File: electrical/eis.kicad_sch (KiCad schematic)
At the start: 7 parts

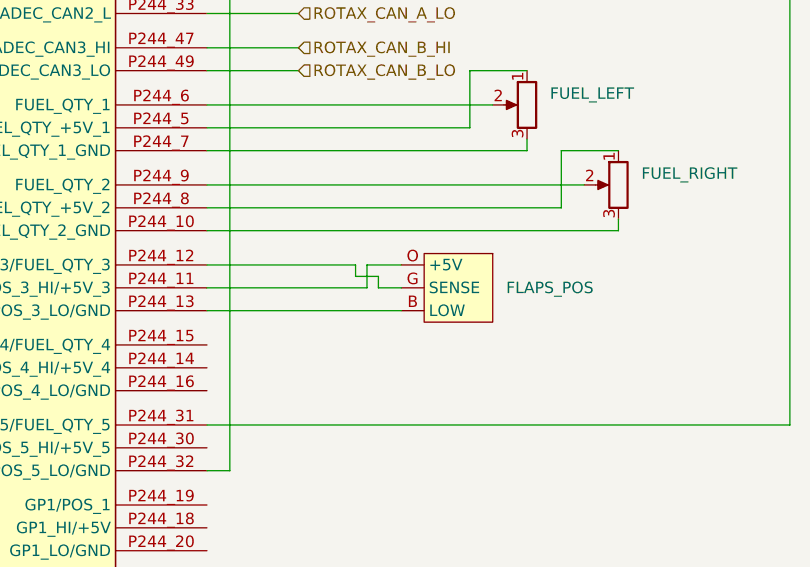
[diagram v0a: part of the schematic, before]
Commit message: Switch Slats to use Roll and put Flaps on Flaps.
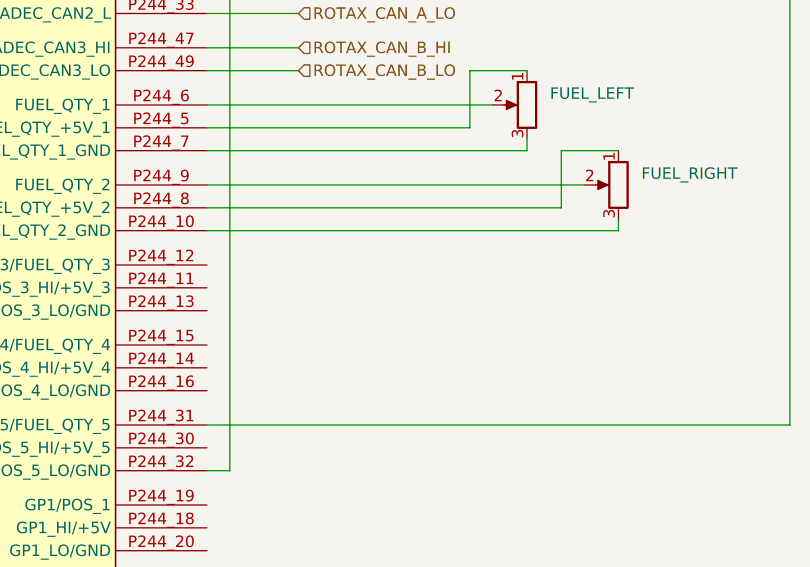
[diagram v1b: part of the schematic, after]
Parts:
- removed FLAPS_POS: ~, symbol flyerx:Ray_Allen_POS-12
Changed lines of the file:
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@@
   (title_block
     (title "EIS")
-    (date "2024-02-13")
-    (rev "0.9.1")
+    (date "2024-03-15")
+    (rev "0.9.2")
     (company "N915SN Angry Bird")
   )
@@
     (stroke (width 0) (type default))
   )
-  (wire (pts (xy 67.31 251.46) (xy 85.09 251.46))
-    (stroke (width 0) (type default))
-  )
   (wire (pts (xy 95.25 33.02) (xy 102.87 33.02))
     (stroke (width 0) (type default))
@@
     (stroke (width 0) (type default))
   )
-  (wire (pts (xy 67.31 254) (xy 88.9 254))
-    (stroke (width 0) (type default))
-  )
   (wire (pts (xy 67.31 190.5) (xy 69.85 190.5))
     (stroke (width 0) (type default))
@@
     (stroke (width 0) (type default))
   )
-  (wire (pts (xy 86.36 251.46) (xy 86.36 250.19))
-    (stroke (width 0) (type default))
-  )
   (wire (pts (xy 67.31 187.96) (xy 137.16 187.96))
     (stroke (width 0) (type default))
@@
     (stroke (width 0) (type default))
   )
-  (wire (pts (xy 86.36 251.46) (xy 88.9 251.46))
-    (stroke (width 0) (type default))
-  )
   (wire (pts (xy 90.17 121.92) (xy 92.71 121.92))
     (stroke (width 0) (type default))
@@
     (stroke (width 0) (type default))
   )
-  (wire (pts (xy 67.31 248.92) (xy 83.82 248.92))
-    (stroke (width 0) (type default))
-  )
   (wire (pts (xy 113.03 245.11) (xy 113.03 243.84))
     (stroke (width 0) (type default))
@@
     (stroke (width 0) (type default))
   )
-  (wire (pts (xy 85.09 248.92) (xy 88.9 248.92))
-    (stroke (width 0) (type default))
-  )
   (wire (pts (xy 67.31 240.03) (xy 109.22 240.03))
     (stroke (width 0) (type default))
@@
     (stroke (width 0) (type default))
   )
-  (wire (pts (xy 83.82 248.92) (xy 83.82 250.19))
-    (stroke (width 0) (type default))
-  )
   (wire (pts (xy 67.31 245.11) (xy 113.03 245.11))
     (stroke (width 0) (type default))
   )
-  (wire (pts (xy 83.82 250.19) (xy 86.36 250.19))
-    (stroke (width 0) (type default))
-  )
   (wire (pts (xy 67.31 220.98) (xy 77.47 220.98))
     (stroke (width 0) (type default))
@@
   )
   (wire (pts (xy 106.68 236.22) (xy 113.03 236.22))
-    (stroke (width 0) (type default))
-  )
-  (wire (pts (xy 85.09 251.46) (xy 85.09 248.92))
     (stroke (width 0) (type default))
   )
@@
     (effects (font (size 1.27 1.27)) (justify left))
   )
-  (symbol (lib_id "flyerx:Ray_Allen_POS-12") (at 99.06 247.65 0) (mirror y) (unit 1)
-    (in_bom yes) (on_board yes) (dnp no)
-    (property "Reference" "FLAPS_POS" (at 105.41 251.46 0)
-      (effects (font (size 1.27 1.27)))
-    )
-    (property "Value" "~" (at 105.41 245.11 0)
-      (effects (font (size 1.27 1.27)))
-    )
-    (property "Footprint" "" (at 105.41 245.11 0)
-      (effects (font (size 1.27 1.27)) hide)
-    )
-    (property "Datasheet" "" (at 105.41 245.11 0)
-      (effects (font (size 1.27 1.27)) hide)
-    )
-    (pin "B")
-    (pin "G")
-    (pin "O")
-    (instances
-      (project "electrical"
-        (path "/e8ec215a-dbe2-4eba-a577-e50a0a128049/72184f52-5cc1-469a-bd6f-4bd63aea59bf"
-          (reference "FLAPS_POS") (unit 1)
-        )
-      )
-    )
-  )
   (symbol (lib_id "flyerx:Kavlico_P4055") (at 100.33 115.57 0) (mirror y) (unit 1)

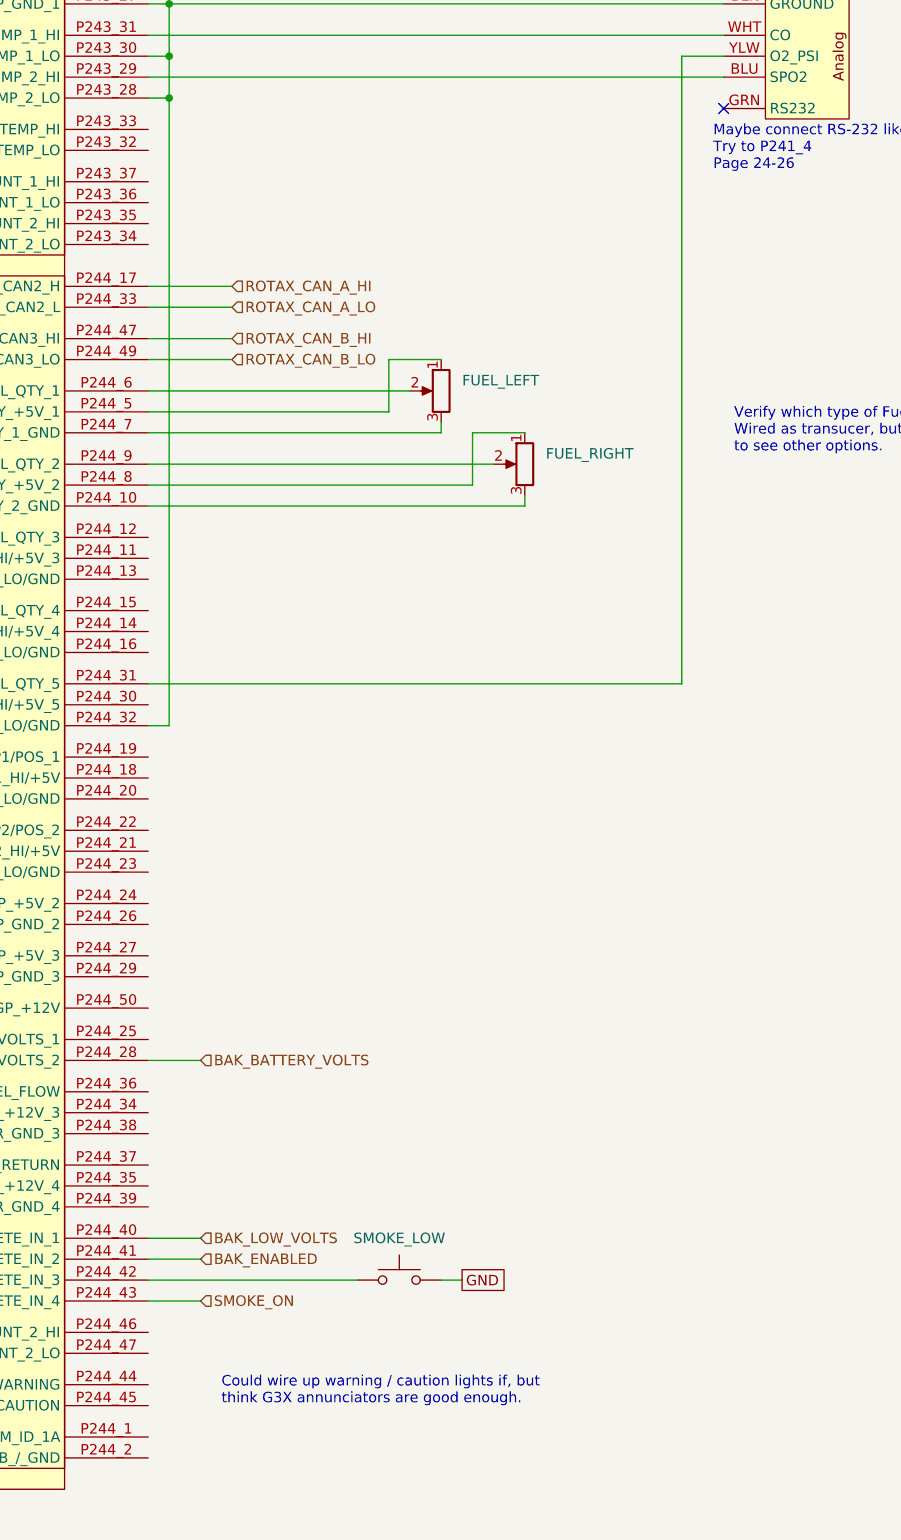
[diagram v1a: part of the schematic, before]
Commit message: Converted to breakers w/GAD 27 instead of VP-X.
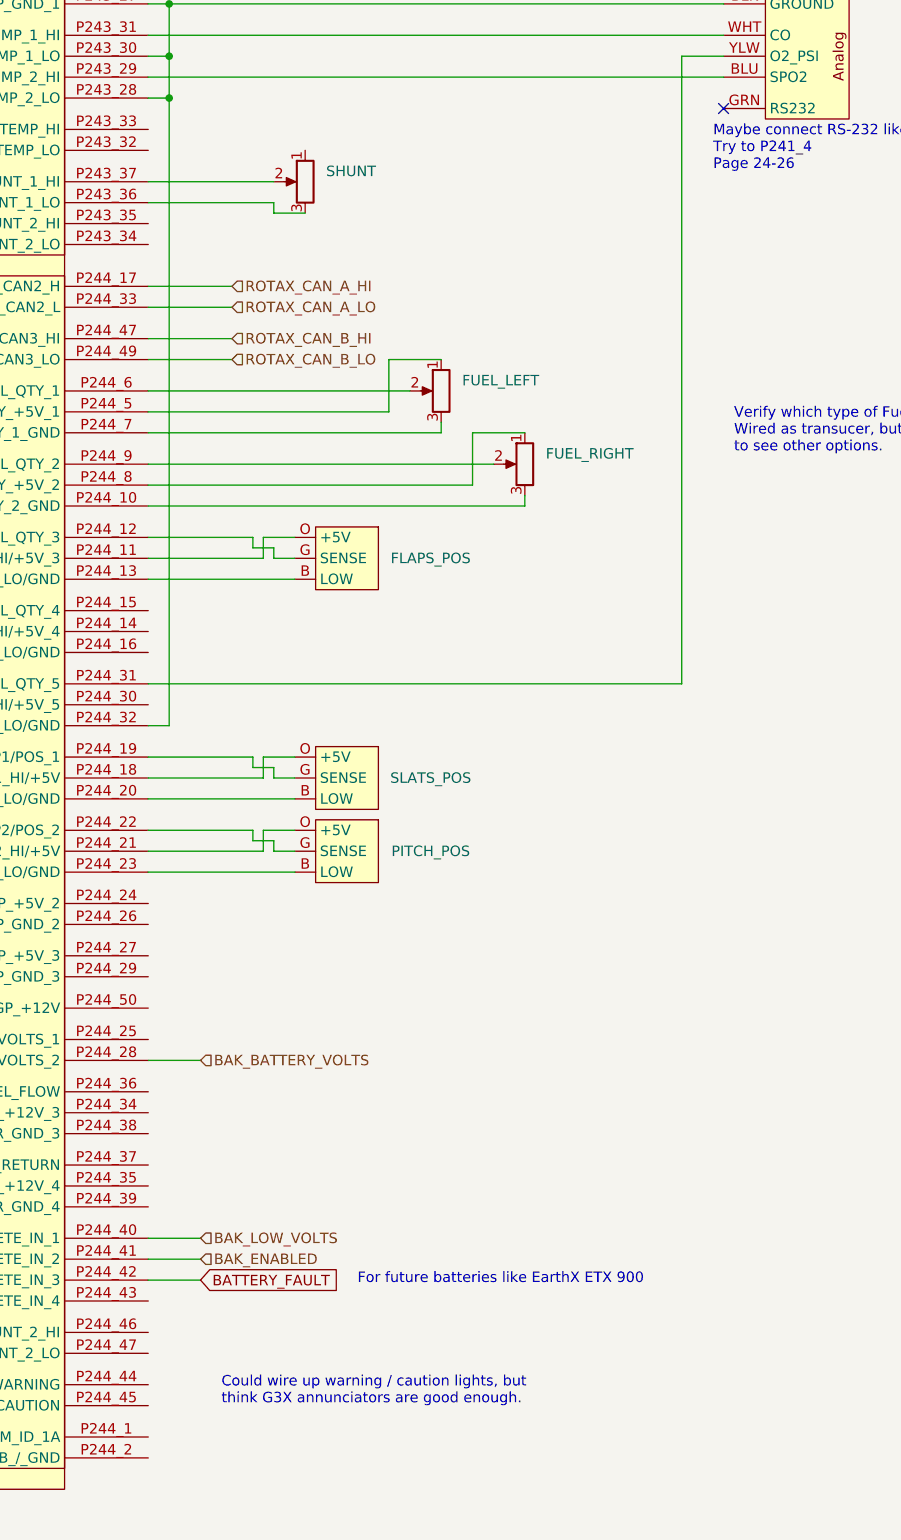
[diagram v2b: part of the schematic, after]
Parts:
- removed SMOKE_LOW: FLOAT_SENSOR, symbol Switch:SW_Push
- added FLAPS_POS, PITCH_POS, SLATS_POS: ~, symbol flyerx:Ray_Allen_POS-12
- added SHUNT: FUEL_QTY_SENSOR, symbol Device:R_Potentiometer
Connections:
- net at GEA24.P243_36 (SHUNT_1_LO): now also SHUNT.3
- net at GEA24.P243_37 (SHUNT_1_HI): now also SHUNT.2
- net at GEA24.P244_11 (POS_3_HI/+5V_3): now also FLAPS_POS.O (+5V)
- net at GEA24.P244_12 (POS_3/GP_3/FUEL_QTY_3): now also FLAPS_POS.G (SENSE)
- net at GEA24.P244_13 (POS_3_LO/GND): now also FLAPS_POS.B (LOW)
- net at GEA24.P244_18 (GP1_HI/+5V): now also SLATS_POS.O (+5V)
- net at GEA24.P244_19 (GP1/POS_1): now also SLATS_POS.G (SENSE)
- net at GEA24.P244_20 (GP1_LO/GND): now also SLATS_POS.B (LOW)
- net at GEA24.P244_21 (GP2_HI/+5V): now also PITCH_POS.O (+5V)
- net at GEA24.P244_22 (GP2/POS_2): now also PITCH_POS.G (SENSE)
- net at GEA24.P244_23 (GP2_LO/GND): now also PITCH_POS.B (LOW)
- net BATTERY_FAULT: now reaches GEA24.P244_42 (DISCRETE_IN_3)
- net SMOKE_ON: no longer names the net of GEA24.P244_43 (DISCRETE_IN_4)
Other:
- note added: "Could wire up warning / caution lights, but think G3X annunciators are good enough."
- note added: "For future batteries like EarthX ETX 900"
- note removed: "Could wire up warning / caution lights if, but think G3X annunciators are good enough."

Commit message: Interim check-in. Not sure what I was doing.
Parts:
- removed FLAPS_POS: ~, symbol flyerx:Ray_Allen_POS-12
- removed FUEL_PRESSURE: ~, symbol flyerx:Kavlico_P4055
- added FUEL_PRESSURE: ~, symbol flyerx:Ray_Allen_POS-12
- added GHA15_DISABLE_SW1: ~, symbol Switch:SW_SPST
- added SMOKE_LOW_SW: FLOAT_SENSOR, symbol Switch:SW_Push
- renumbered PITCH_POS to FLAPS_POS, SLATS_POS to PITCH_POS
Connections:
- net GND: now also GHA15_DISABLE_SW1.2 (B), SMOKE_LOW_SW.2
- net at SHUNT.2: now also GEA24.P243_35 (SHUNT_2_HI); no longer GEA24.P243_37 (SHUNT_1_HI)
- net at SHUNT.3: now also GEA24.P243_34 (SHUNT_2_LO); no longer GEA24.P243_36 (SHUNT_1_LO)
- net at GEA24.P243_1 (FUEL_PRESS_GND): now also FUEL_PRESSURE.B (LOW)
- net at GEA24.P243_4 (FUEL_PRESS_XDCR_+5V): now also FUEL_PRESSURE.O (+5V)
- net at GEA24.P243_2 (FUEL_PRESS): now also FUEL_PRESSURE.G (SENSE)
- net at FUEL_RIGHT.1: now also GEA24.P244_35 (FUEL_XDCR_+12V_4); no longer GEA24.P244_8 (FUEL_QTY_+5V_2)
- net at FUEL_RIGHT.3: no longer GEA24.P244_10 (FUEL_QTY_2_GND)
- net at FUEL_LEFT.1: now also GEA24.P244_34 (FUEL_XDCR_+12V_3); no longer GEA24.P244_5 (FUEL_QTY_+5V_1)
- net at FUEL_LEFT.3: no longer GEA24.P244_7 (FUEL_QTY_1_GND)
- net at GEA24.P243_26 (GP+5V_1): no longer CO.RED (+5V)
- net at GEA24.P243_29 (POS_7/TIT_2/MISC_TEMP_2_HI): no longer CO.BLU (SPO2)
- net at GEA24.P243_31 (POS_6/TIT_1/MISC_TEMP_1_HI): no longer CO.WHT (CO)
- net at GEA24.P244_11 (POS_3_HI/+5V_3): now also CO.RED (+5V)
- net at GEA24.P244_12 (POS_3/GP_3/FUEL_QTY_3): now also CO.WHT (CO)
- net at GEA24.P244_13 (POS_3_LO/GND): now also CO.BLK (GROUND)
- net at GEA24.P244_31 (POS_5/GP_5/FUEL_QTY_5): no longer CO.YLW (O2_PSI)
- net at GEA24.P244_43 (DISCRETE_IN_4): now also GHA15_DISABLE_SW1.1 (A)
- net BATTERY_FAULT: no longer names the net of GEA24.P244_42 (DISCRETE_IN_3)
- net BATTERY_FAULT: now also SMOKE_LOW_SW.1
- removed net ROTAX_CAN_B_HI: GEA24.P244_47 (SHUNT_2_LO)
- net ROTAX_CAN_B_LO: no longer names the net of GEA24.P244_49 (FADEC_CAN3_LO)
- now unconnected: GEA24.P243_27 (GP_GND_1), GEA24.P243_28 (POS_7/TIT_2/MISC_TEMP_2_LO), GEA24.P243_30 (POS_6/TIT_1/MISC_TEMP_1_LO), GEA24.P244_32 (POS_5_LO/GND)
- no-connect marks 1 -> 11
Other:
- note added: "Configured as FADEC inputs Manifold Temp"
- note added: "Decide which inputs to use between battery backup, smoke, GHA15 disabled or battery fault"
- note added: "Need to see what Zlin connected on J241"
- note added: "Not sure where fuel ground is coming from and if 34 or 35 goes left/right"
- note added: "Not sure why didn't connect them separately"
- note added: "See if there is a shunt to connect to"
- note removed: "Could wire up warning / caution lights, but think G3X annunciators are good enough."
- note removed: "For future batteries like EarthX ETX 900"
- note removed: "Maybe connect RS-232 like CO Detector Try to P241_4 Page 24-26"
- note removed: "Verify which type of Fuel Sensor. Wired as transucer, but check out page 26-8 to see other options."
- moved on the sheet: CO, FUEL_LEFT, FUEL_RIGHT, SHUNT

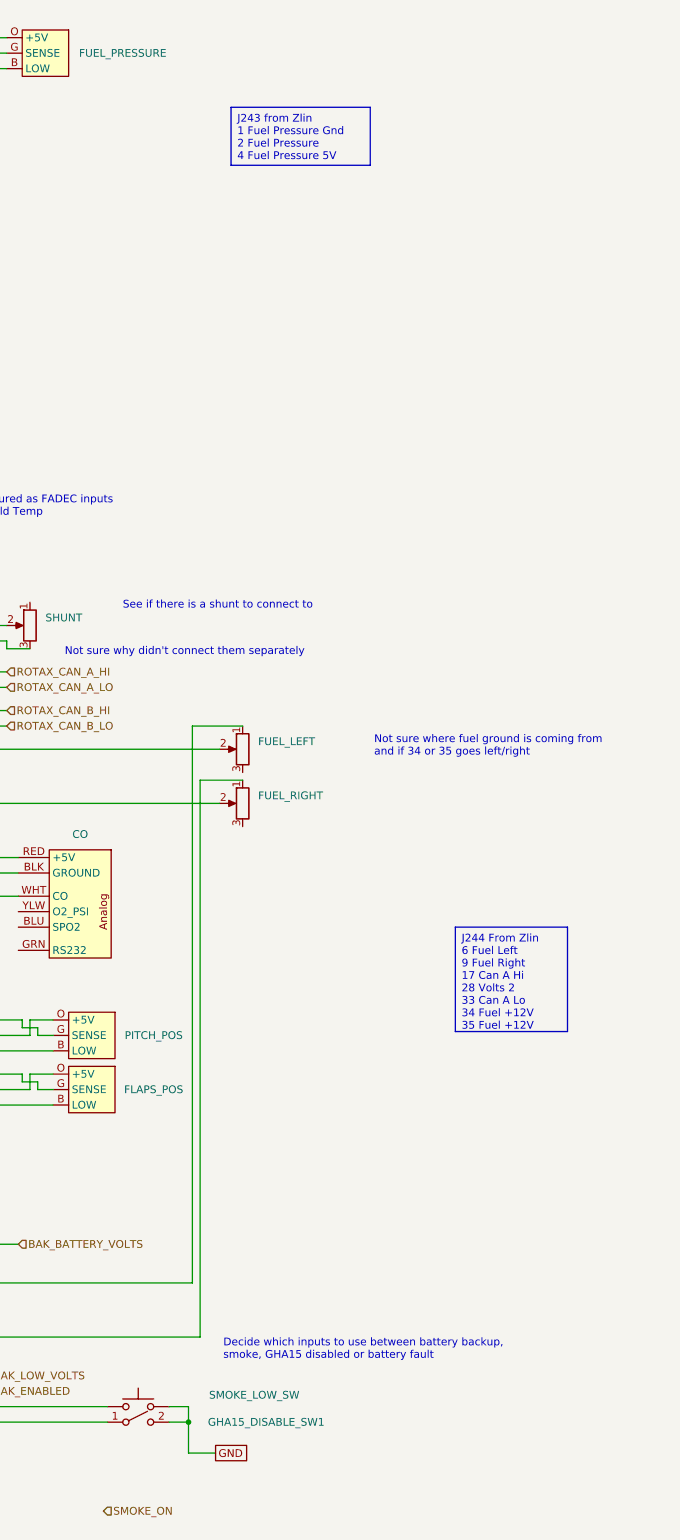
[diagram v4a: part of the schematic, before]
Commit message: Cleaned up power and smoke.
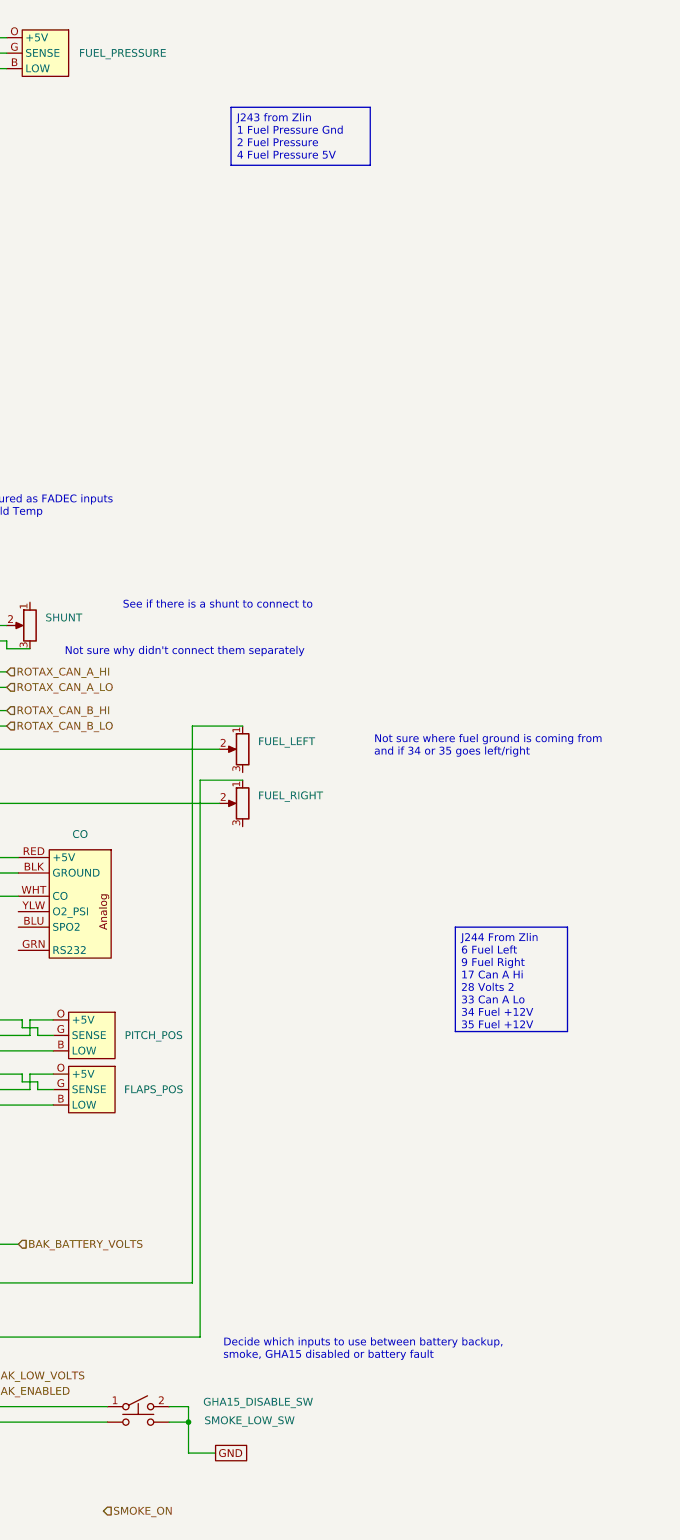
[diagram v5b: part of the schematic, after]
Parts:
- renumbered GHA15_DISABLE_SW1 to GHA15_DISABLE_SW
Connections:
- net at GHA15_DISABLE_SW.1 (A): now also GEA24.P244_42 (DISCRETE_IN_3); no longer GEA24.P244_43 (DISCRETE_IN_4)
- net at SMOKE_LOW_SW.1: now also GEA24.P244_43 (DISCRETE_IN_4); no longer GEA24.P244_42 (DISCRETE_IN_3)
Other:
- moved on the sheet: GHA15_DISABLE_SW, SMOKE_LOW_SW
